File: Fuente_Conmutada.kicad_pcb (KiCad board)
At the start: 2 copper layers, 140 x 95 mm, 50 parts, among them J1 Terminal_220v, J2 Terminal_12v, J3 Vout, Q1 IRF840, Q2 IRF840, T1 Transformer_1P_SS, U1 TL494, U2 IR2110

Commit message: fidu
Se agregaron los fiduciales
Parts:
- added REF**: Fiducial_1.5mm, Fiducial:Fiducial_1.5mm_Mask3mm, F.Cu at (194.2, 47.1)
- added REF**: Fiducial_1.5mm, Fiducial:Fiducial_1.5mm_Mask3mm, F.Cu at (95.2, 47.1)
- added REF**: Fiducial_1.5mm, Fiducial:Fiducial_1.5mm_Mask3mm, F.Cu at (80.4, 116.4)
- added REF**: Fiducial_1.5mm, Fiducial:Fiducial_1.5mm_Mask3mm, F.Cu at (197.7, 129.9)

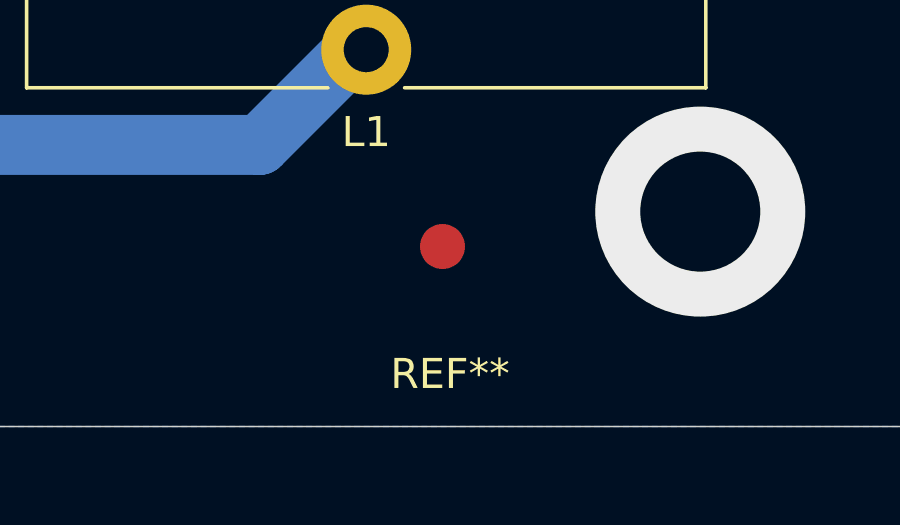
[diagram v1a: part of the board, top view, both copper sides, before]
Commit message: cambio
saque un fidu
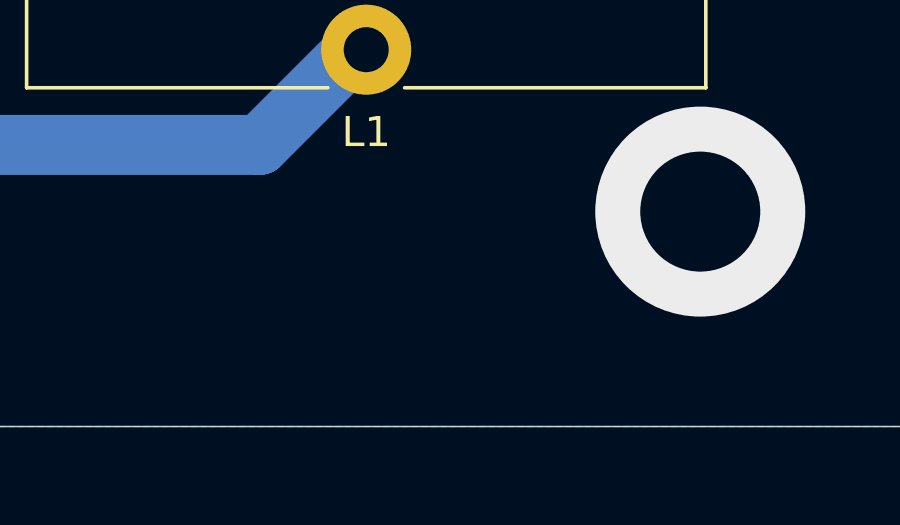
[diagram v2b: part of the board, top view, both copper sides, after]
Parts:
- removed the REF** at (197.7, 129.9)
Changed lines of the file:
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@@
 			(outputformat 1)
 			(mirror no)
-			(drillshape 1)
+			(drillshape 0)
 			(scaleselection 1)
 			(outputdirectory "")
@@
 		)
 	)
-	(footprint "Fiducial:Fiducial_1.5mm_Mask3mm"
-		(layer "F.Cu")
-		(at 197.653 129.892)
-		(descr "Circular Fiducial, 1.5mm bare copper, 3mm soldermask opening")
-		(tags "fiducial")
-		(property "Reference" "REF**"
-			(at 0.25 4.25 0)
-			(layer "F.SilkS")
-			(effects
-				(font
-					(size 1 1)
-					(thickness 0.15)
-				)
-			)
-		)
-		(property "Value" "Fiducial_1.5mm"
-			(at 0 2.6035 0)
-			(layer "F.Fab")
-			(effects
-				(font
-					(size 1 1)
-					(thickness 0.15)
-				)
-			)
-		)
-		(property "Footprint" "Fiducial:Fiducial_1.5mm_Mask3mm"
-			(at 0 0 0)
-			(unlocked yes)
-			(layer "F.Fab")
-			(hide yes)
-			(effects
-				(font
-					(size 1.27 1.27)
-					(thickness 0.15)
-				)
-			)
-		)
-		(property "Datasheet" ""
-			(at 0 0 0)
-			(unlocked yes)
-			(layer "F.Fab")
-			(hide yes)
-			(effects
-				(font
-					(size 1.27 1.27)
-					(thickness 0.15)
-				)
-			)
-		)
-		(property "Description" ""
-			(at 0 0 0)
-			(unlocked yes)
-			(layer "F.Fab")
-			(hide yes)
-			(effects
-				(font
-					(size 1.27 1.27)
-					(thickness 0.15)
-				)
-			)
-		)
-		(attr smd)
-		(fp_circle
-			(center 0 0)
-			(end 1.75 0)
-			(stroke
-				(width 0.05)
-				(type solid)
-			)
-			(fill none)
-			(layer "F.CrtYd")
-		)
-		(fp_circle
-			(center 0 0)
-			(end 1.5 0)
-			(stroke
-				(width 0.1)
-				(type solid)
-			)
-			(fill none)
-			(layer "F.Fab")
-		)
-		(fp_text user "${REFERENCE}"
-			(at 0 0 0)
-			(layer "F.Fab")
-			(effects
-				(font
-					(size 0.4 0.4)
-					(thickness 0.06)
-				)
-			)
-		)
-		(pad "" smd circle
-			(at 0 0)
-			(size 1.5 1.5)
-			(layers "F.Cu" "F.Mask")
-			(solder_mask_margin 0.75)
-			(clearance 0.75)
-		)
-	)
